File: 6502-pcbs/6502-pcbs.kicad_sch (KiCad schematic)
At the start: 0 parts

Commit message: initial 6502 schematic
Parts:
- added C3: 1uF, symbol Device:C_Small_US
- added C4, C5, C8: 0.1uF, symbol Device:C_Small
- added C6, C7, C9: 0.01uF, symbol Device:C_Small
- added D1: RED, symbol Device:LED
- added D3, D4, D5: YELLOW, symbol Device:LED
- added R1, R2, R3, R5, R6, R7: 1k, symbol Device:R_Small_US
- added R10, R11, R8, R9: 220, symbol Device:R_Small_US
- added R4: 1M, symbol Device:R_Small_US
- added RV1: 10k?, symbol Device:R_Potentiometer_US
- added RV2: 1M, symbol Device:R_Potentiometer_US
- added SW1, SW2: Push, symbol Switch:SW_Push
- added SW3: SW_SPDT, symbol Switch:SW_SPDT
- added U1: W65C02SxP, Package_DIP:DIP-40_W15.24mm, symbol 65xx-library:W65C02SxP
- added U10: 74LS08, symbol 74xx:74LS08
- added U11: 74LS04, symbol 74xx:74LS04
- added U12: 74LS32, symbol 74xx:74LS32
- added U2: HM62256BLP, Package_DIP:DIP-28_W15.24mm, symbol Memory_RAM:HM62256BLP
- added U3: 28C256, symbol Memory_EEPROM:28C256
- added U4: W65C22SxP, Package_DIP:DIP-40_W15.24mm, symbol 65xx-library:W65C22SxP
- added U5: RC1602A, Display:RC1602A, symbol Display_Character:RC1602A
- added U6: W65C51NxP, Package_DIP:DIP-28_W15.24mm, symbol 65xx-library:W65C51NxP
- added U7, U8, U9: NE555P, Package_DIP:DIP-8_W7.62mm, symbol Timer:NE555P
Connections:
- new net: U4.13 (PB3), U5.10 (DB3)
- new net: U4.14 (PB4), U5.11 (DB4)
- new net: U4.15 (PB5), U5.12 (DB5)
- new net: U4.16 (PB6), U5.13 (DB6)
- new net: U4.17 (PB7), U5.14 (DB7)
- new net: RV1.2, U5.3 (VO)
- new net: U4.7 (PA5), U5.4 (RS)
- new net: U4.8 (PA6), U5.5 (R/W)
- new net: U4.9 (PA7), U5.6 (E)
- new net: U4.10 (PB0), U5.7 (DB0)
- new net: U4.11 (PB1), U5.8 (DB1)
- new net: U4.12 (PB2), U5.9 (DB2)
- new net: D4.1 (K), R10.1
- new net: R6.2, SW3.1 (A), U9.2 (TR)
- new net: D5.1 (K), R11.1
- new net: C8.1, R4.2, U8.6 (THR), U8.7 (DIS)
- new net: R5.2, SW2.2, U8.2 (TR)
- new net: D3.2 (A), U10.5, U8.3 (Q)
- new net: C7.1, U8.5 (CV)
- new net: U10.3, U12.1
- new net: U10.6, U12.2
- new net: U10.9, U12.3
- new net: D5.2 (A), U10.2, U11.1, U9.3 (Q)
- new net: U10.4, U11.2
- new net: R2.2, R3.1, U7.7 (DIS)
- new net: U1.10 (A1), U2.9 (A1), U3.9 (A1)
- new net: U1.11 (A2), U2.8 (A2), U3.8 (A2)
- new net: U1.12 (A3), U2.7 (A3), U3.7 (A3)
- new net: U1.13 (A4), U2.6 (A4), U3.6 (A4)
- new net: U1.14 (A5), U2.5 (A5), U3.5 (A5)
- new net: U1.15 (A6), U2.4 (A6), U3.4 (A6)
- new net: U1.16 (A7), U2.3 (A7), U3.3 (A7)
- new net: U1.17 (A8), U2.25 (A8), U3.25 (A8)
- new net: U1.18 (A9), U2.24 (A9), U3.24 (A9)
- new net: U1.19 (A10), U2.21 (A10), U3.21 (A10)
- new net: U1.20 (A11), U2.23 (A11), U3.23 (A11)
- new net: U1.22 (A12), U2.2 (A12), U3.2 (A12)
- new net: U1.23 (A13), U2.26 (A13), U3.26 (A13)
- new net: U1.24 (A14), U2.1 (A14), U3.1 (A14)
- new net: U1.26 (D7), U2.19 (Q7), U3.19 (D7), U4.26 (D7)
- new net: U1.27 (D6), U2.18 (Q6), U3.18 (D6), U4.27 (D6)
- new net: U1.28 (D5), U2.17 (Q5), U3.17 (D5), U4.28 (D5)
- new net: U1.29 (D4), U2.16 (Q4), U3.16 (D4), U4.29 (D4)
- new net: U1.30 (D3), U2.15 (Q3), U3.15 (D3), U4.30 (D3)
- new net: U1.31 (D2), U2.13 (Q2), U3.13 (D2), U4.31 (D2)
- new net: U1.32 (D1), U2.12 (Q1), U3.12 (D1), U4.32 (D1)
- new net: U1.33 (D0), U2.11 (Q0), U3.11 (D0), U4.33 (D0)
- new net: R1.2, SW1.2, U1.40 (~{RES})
- new net: U1.9 (A0), U2.10 (A0), U3.10 (A0)
- new net: D3.1 (K), R9.1
- new net: D1.1 (K), R8.1
- new net: R7.2, SW3.3 (C), U9.4 (R)
- new net: R3.2, RV2.2
- new net: C3.1, RV2.3, U7.2 (TR), U7.6 (THR)
- new net: C9.1, U9.5 (CV)
- new net: C6.1, U7.5 (CV)
- new net: D4.2 (A), U10.1, U7.3 (Q)
- new net: U10.10, U11.4
- new net +5V: C4.1, C5.1, R1.1, R2.1, R4.1, R5.1, R6.1, R7.1, U1.2 (RDY), U1.36 (BE), U1.38 (~{SO}), U1.4 (~{IRQ}), U1.6 (~{NMI}), U1.8 (VDD), U2.28 (VCC), U3.28 (VCC), U4.20 (VCC), U5.15 (A/VEE), U5.2 (VDD), U7.4 (R), U7.8 (VCC), U8.4 (R), U8.8 (VCC), U9.8 (VCC)
- new net CLK: D1.2 (A), U1.37 (ϕ0), U10.8, U11.5
- new net GND: C3.2, C4.2, C5.2, C6.2, C7.2, C8.2, C9.2, R10.2, R11.2, R8.2, R9.2, RV1.3, SW1.1, SW2.1, U1.21 (VSS), U2.14 (GND), U3.14 (GND), U4.1 (VSS), U5.1 (VSS), U5.16 (K), U6.1 (VSS), U7.1 (GND), U8.1 (GND), U9.1 (GND), U9.6 (THR)
- new net HALT: U11.3
- new net ~{CLK}: U11.6
- no-connect marks 0 -> 19

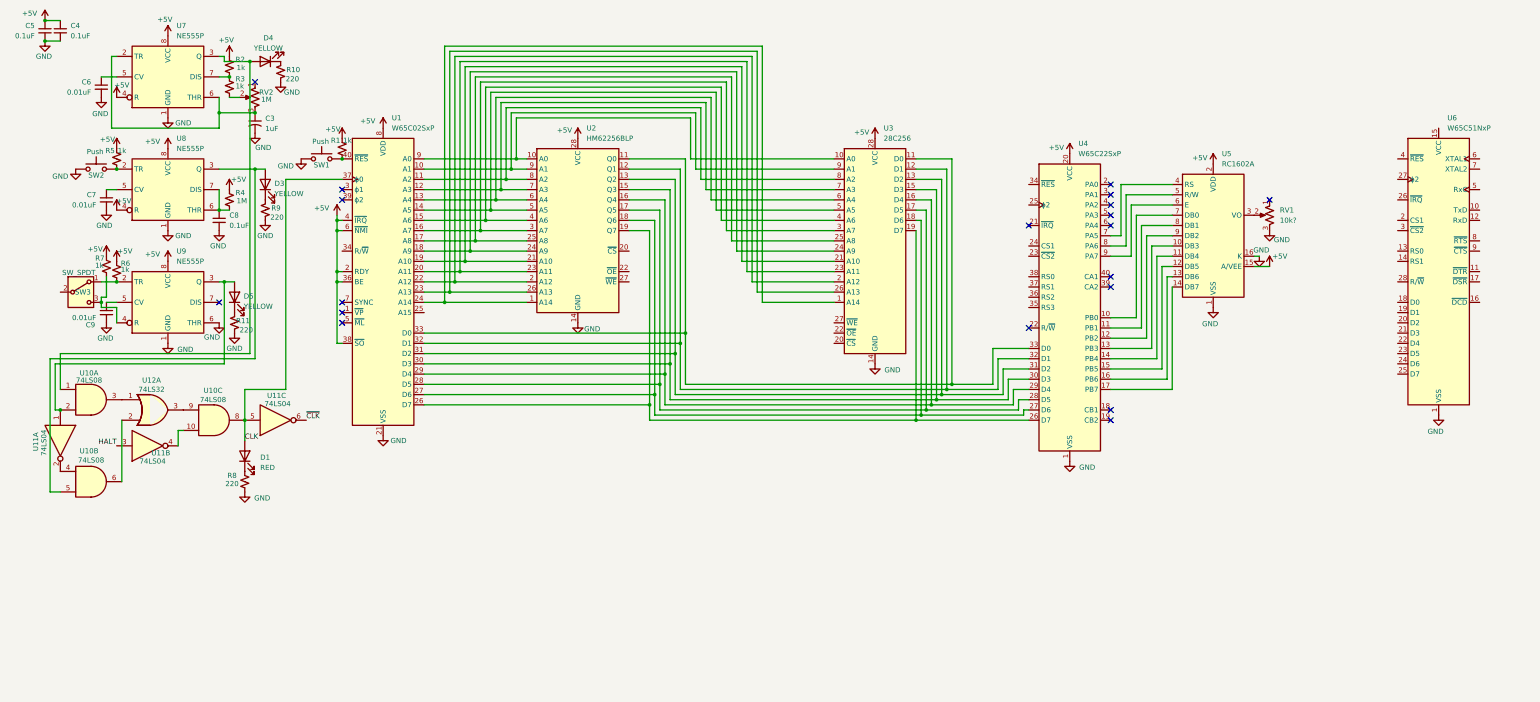
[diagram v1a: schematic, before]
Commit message: datasheets and bus timing
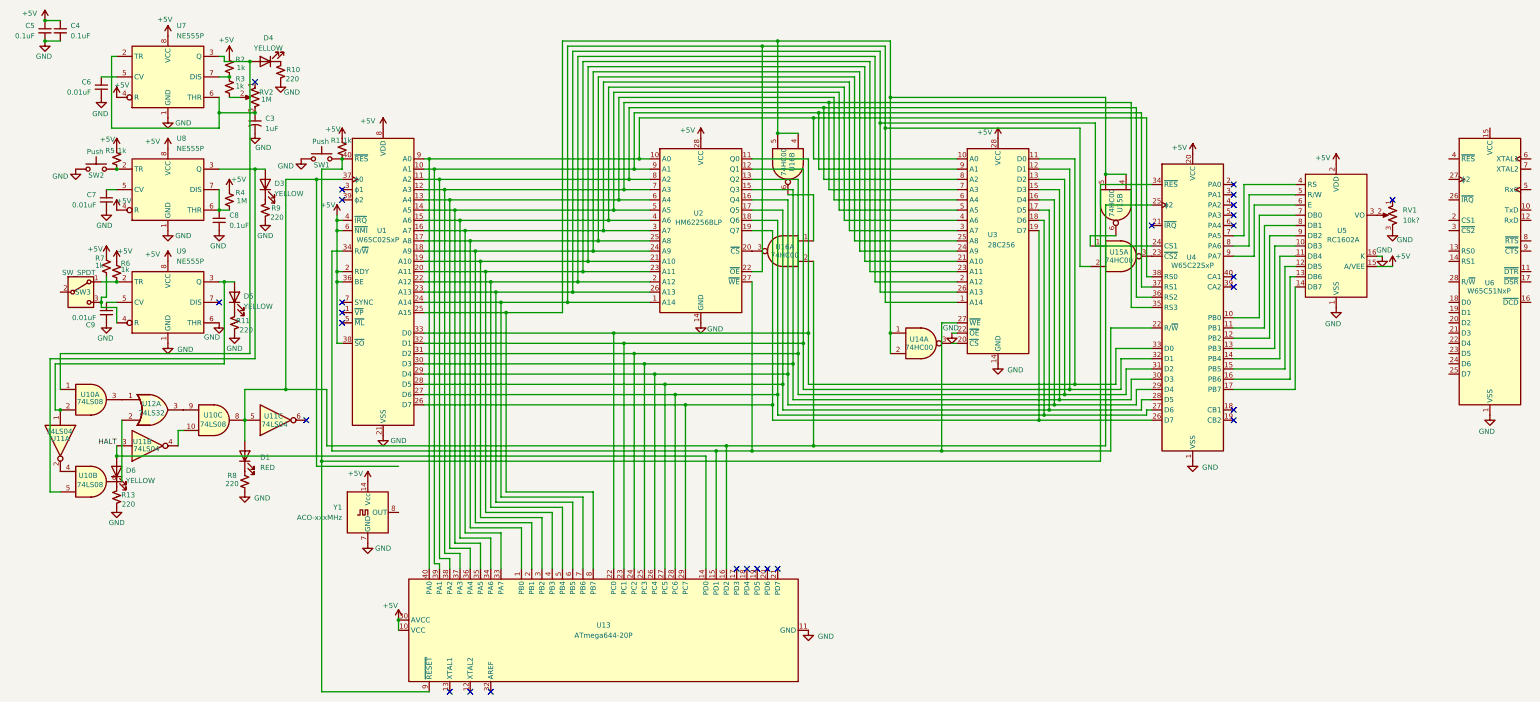
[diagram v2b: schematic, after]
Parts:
- added D6: YELLOW, LED_THT:LED_D5.0mm_Horizontal_O6.35mm_Z9.0mm, symbol Device:LED
- added R13: 220, Resistor_THT:R_Axial_DIN0309_L9.0mm_D3.2mm_P12.70mm_Horizontal, symbol Device:R_Small_US
- added U13: ATmega644-20P, Package_DIP:DIP-40_W15.24mm, symbol MCU_Microchip_ATmega:ATmega644-20P
- added U14, U15, U16: 74HC00, Package_DIP:DIP-14_W7.62mm, symbol 74xx:74HC00
- added Y1: ACO-xxxMHz, Oscillator:Oscillator_DIP-14, symbol Oscillator:ACO-xxxMHz
- C3: footprint (none) -> Capacitor_THT:CP_Axial_L10.0mm_D4.5mm_P15.00mm_Horizontal
- C4, C5, C6, C7, C8, C9: footprint (none) -> Capacitor_THT:CP_Radial_D4.0mm_P1.50mm
- D1, D3, D4, D5: footprint (none) -> LED_THT:LED_D5.0mm_Horizontal_O6.35mm_Z9.0mm
- R1, R10, R11, R2, R3, R4, R5, R6, R7, R8, R9: footprint (none) -> Resistor_THT:R_Axial_DIN0309_L9.0mm_D3.2mm_P12.70mm_Horizontal
- RV1, RV2: footprint (none) -> Potentiometer_THT:Potentiometer_Bourns_3386C_Horizontal
- SW1, SW2: footprint (none) -> Button_Switch_THT:SW_PUSH_6mm
- SW3: footprint (none) -> Button_Switch_SMD:SW_SPDT_PCM12
- U10, U11, U12: footprint (none) -> Package_DIP:DIP-14_W7.62mm
- U3: footprint (none) -> Package_DIP:DIP-28_W15.24mm
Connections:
- net CLK is gone; now on an unnamed net: D1.2 (A), U1.37 (ϕ0), U10.8, U11.5
- net +5V: now also U13.10 (VCC), U13.30 (AVCC), Y1.14 (Vcc)
- net GND: now also U3.22 (~{OE}), R13.2, U13.11 (GND), U13.31 (GND), Y1.7 (GND)
- net HALT: now also D6.2 (A), U13.14 (PD0)
- net at U1.10 (A1), U2.9 (A1), U3.9 (A1): now also U4.37 (RS1), U13.39 (PA1)
- net at U1.11 (A2), U2.8 (A2), U3.8 (A2): now also U4.36 (RS2), U13.38 (PA2)
- net at U1.12 (A3), U2.7 (A3), U3.7 (A3): now also U4.35 (RS3), U13.37 (PA3)
- net at U1.13 (A4), U2.6 (A4), U3.6 (A4): now also U13.36 (PA4)
- net at U1.14 (A5), U2.5 (A5), U3.5 (A5): now also U13.35 (PA5)
- net at U1.15 (A6), U2.4 (A6), U3.4 (A6): now also U13.34 (PA6)
- net at U1.16 (A7), U2.3 (A7), U3.3 (A7): now also U13.33 (PA7)
- net at U1.17 (A8), U2.25 (A8), U3.25 (A8): now also U13.1 (PB0)
- net at U1.18 (A9), U2.24 (A9), U3.24 (A9): now also U13.2 (PB1)
- net at U1.19 (A10), U2.21 (A10), U3.21 (A10): now also U13.3 (PB2)
- net at U1.20 (A11), U2.23 (A11), U3.23 (A11): now also U13.4 (PB3)
- net at U1.22 (A12), U2.2 (A12), U3.2 (A12): now also U13.5 (PB4)
- net at U1.23 (A13), U2.26 (A13), U3.26 (A13): now also U4.24 (CS1), U13.6 (PB5)
- net at U1.24 (A14), U2.1 (A14), U3.1 (A14): now also U2.22 (~{OE}), U13.7 (PB6), U15.2
- net at U1.25 (A15): now also U13.8 (PB7), U14.1, U14.2, U15.4, U15.5, U16.4, U16.5
- net at U1.26 (D7), U2.19 (Q7), U3.19 (D7)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: now also U13.29 (PC7)
- net at U1.27 (D6), U2.18 (Q6), U3.18 (D6)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: now also U13.28 (PC6)
- net at U1.28 (D5), U2.17 (Q5), U3.17 (D5)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: now also U13.27 (PC5)
- net at U1.29 (D4), U2.16 (Q4), U3.16 (D4)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: now also U13.26 (PC4)
- net at U1.30 (D3), U2.15 (Q3), U3.15 (D3)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: now also U13.25 (PC3)
- net at U1.31 (D2), U2.13 (Q2), U3.13 (D2)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: now also U13.24 (PC2)
- net at U1.32 (D1), U2.12 (Q1), U3.12 (D1)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: now also U13.23 (PC1)
- net at U1.33 (D0), U2.11 (Q0), U3.11 (D0)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: now also U13.22 (PC0)
- net at U1.34 (R/~{W}): now also U2.27 (~{WE}), U3.27 (~{WE}), U4.22 (R/~{W}), U13.15 (PD1)
- net at R1.2, SW1.2, U1.40 (~{RES}): now also U4.34 (~{RES}), U13.9 (~{RESET})
- net at U1.9 (A0), U2.10 (A0), U3.10 (A0): now also U4.38 (RS0), U13.40 (PA0)
- net at U2.20 (~{CS}): now also U16.3
- net at U4.23 (~{CS2}): now also U15.3
- net at U4.25 (ϕ2): now also U13.16 (PD2), U16.2
- net at U3.20 (~{CS}): now also U14.3
- net ~{CLK}: no longer names the net of U11.6
- new net: U16.1, U16.6
- new net: U15.1, U15.6
- new net: D6.1 (K), R13.1
- no-connect marks 19 -> 27
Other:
- moved on the sheet: RV1, U2, U3, U4, U5, U6

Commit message: even more pcb
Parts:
- added SW4: SW_SPDT, Button_Switch_SMD:SW_SPDT_PCM12, symbol Switch:SW_SPDT
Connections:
- net +5V: no longer U1.4 (~{IRQ}), U1.6 (~{NMI})
- net GND: now also SW3.2 (B)
- net at U1.37 (ϕ0), U13.16 (PD2), U16.2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: now also SW4.2 (B); no longer D1.2 (A), U10.8, U11.5
- net at Y1.8 (OUT): now also SW4.3 (C)
- net at U13.17 (PD3): now also U1.6 (~{NMI})
- net at U13.18 (PD4): now also U1.4 (~{IRQ}), U4.21 (~{IRQ})
- new net: D1.2 (A), SW4.1 (A), U10.8, U11.5
- no-connect marks 27 -> 24
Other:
- moved on the sheet: Y1
